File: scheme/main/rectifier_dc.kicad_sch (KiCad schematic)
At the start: 11 parts, among them K1 G2RL-1-E, Q2 BC847

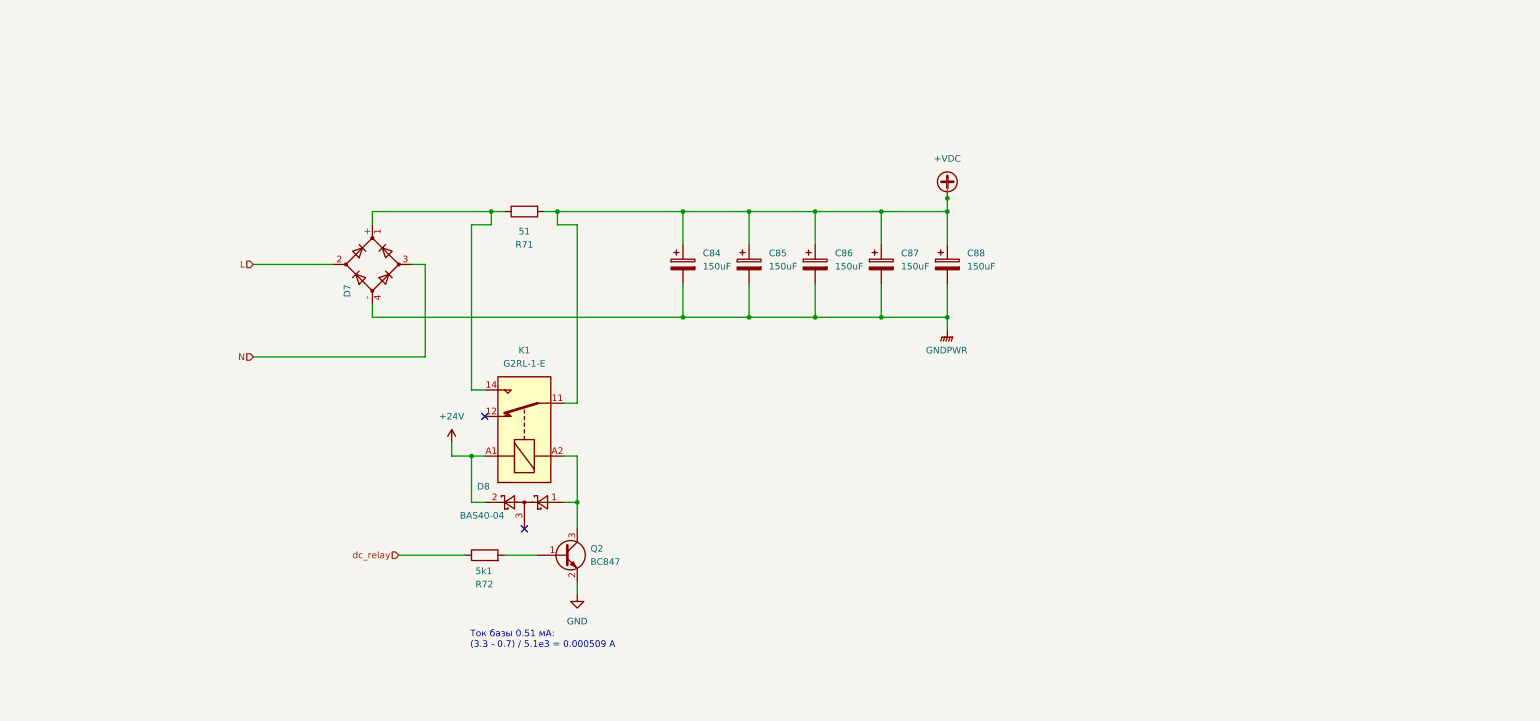
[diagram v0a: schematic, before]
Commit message: drossel in dc+ rail scheme
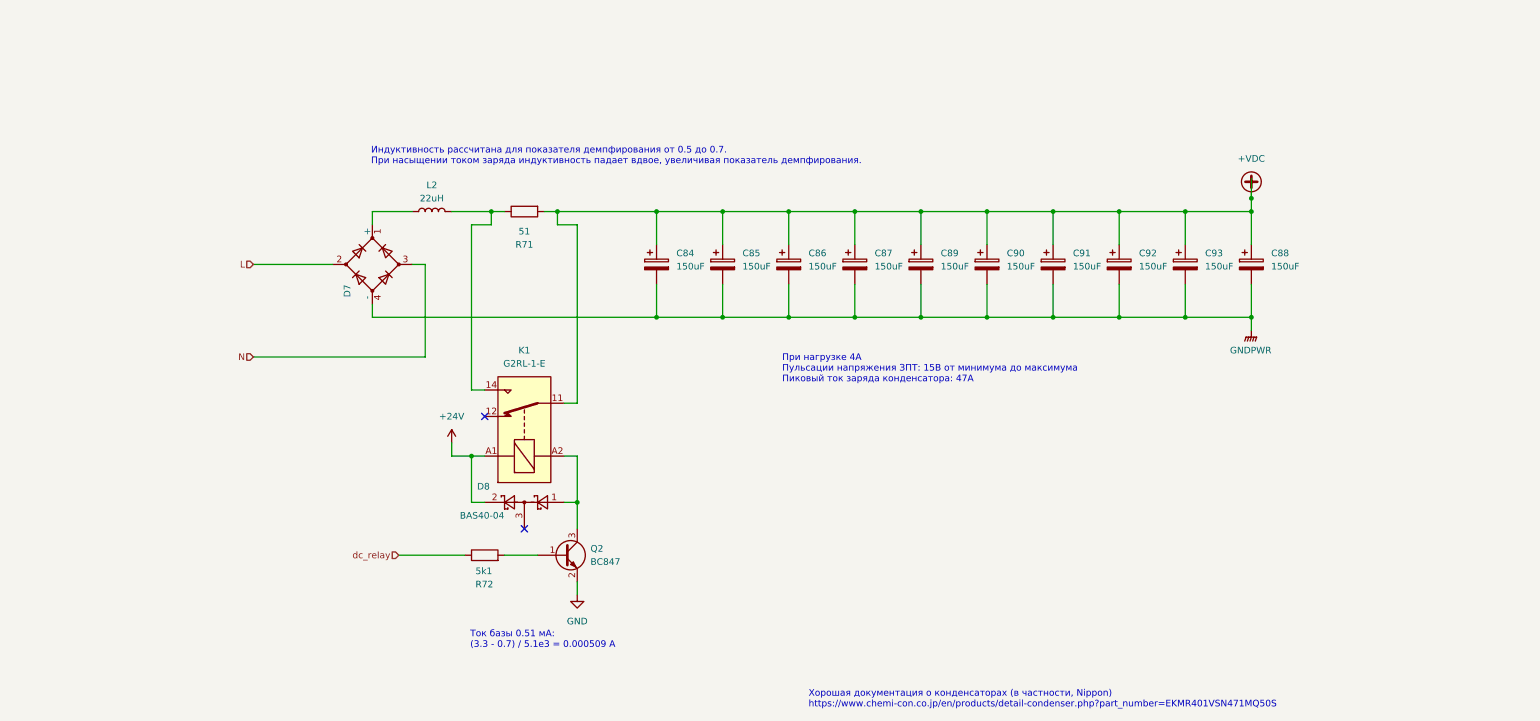
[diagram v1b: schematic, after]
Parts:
- added C89, C90, C91, C92, C93: 150uF, Capacitor_THT:CP_Radial_D30.0mm_P10.00mm_SnapIn, symbol Device:C_Polarized
- added L2: 22uH, Inductor_SMD:L_Vishay_IHLP-6767, symbol Device:L
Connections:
- net +VDC: now also C89.1, C90.1, C91.1, C92.1, C93.1
- net GNDPWR: now also C89.2, C90.2, C91.2, C92.2, C93.2
- net at K1.14, R71.1: now also L2.2; no longer D7.1 (+)
- new net: D7.1 (+), L2.1
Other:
- note added: "Индуктивность рассчитана для показателя демпфирования от 0.5 до 0.7. При насыщении током заряда индуктивность падает вдвое, увеличивая показатель демпфирования."
- note added: "При нагрузке 4А Пульсации напряжения ЗПТ: 15В от минимума до максимума Пиковый ток заряда конденсатора: 47А"
- note added: "Хорошая документация о конденсаторах (в частности, Nippon) https://www.chemi-con.co.jp/en/products/detail-condenser.php?part_number=EKMR401VSN471MQ50S"
- moved on the sheet: C84, C85, C86, C87, C88

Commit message: digital in & out schematic
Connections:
- net +24V: now also D8.3
- no-connect marks 2 -> 1
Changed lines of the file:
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@@
+	)
+	(junction
+		(at 116.84 121.92)
+		(diameter 0)
+		(color 0 0 0 0)
 	)
 	(junction
@@
 		(diameter 0)
 		(color 0 0 0 0)
-	)
-	(no_connect
-		(at 124.46 127)
 	)
 	(no_connect
@@
 	(wire
 		(pts
+			(xy 124.46 127) (xy 116.84 127)
+		)
+		(stroke
+			(width 0)
+			(type default)
+		)
+	)
+	(wire
+		(pts
 			(xy 149.86 86.36) (xy 149.86 80.01)
 		)
@@
 		)
 		(stroke
+			(width 0)
+			(type default)
+		)
+	)
+	(wire
+		(pts
+			(xy 116.84 127) (xy 116.84 121.92)
+		)
+		(stroke

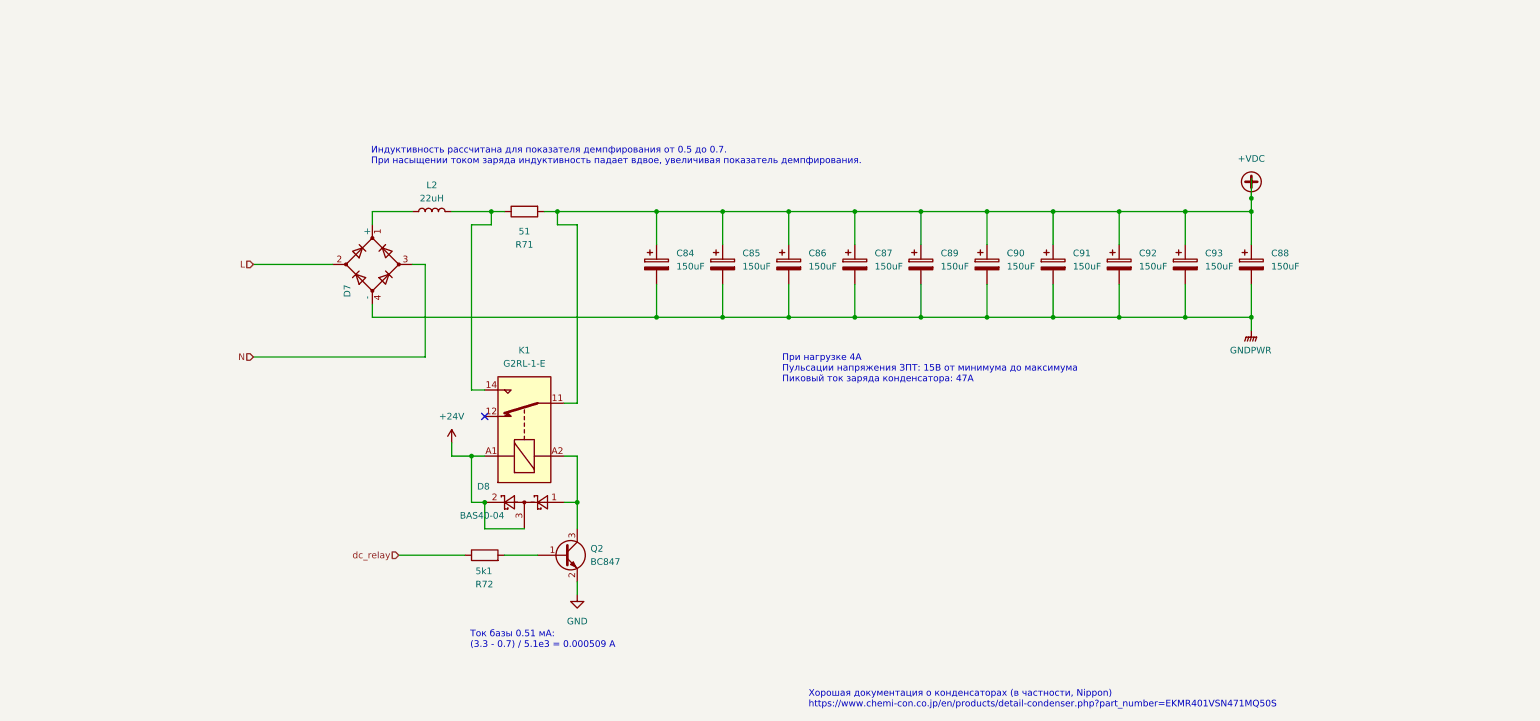
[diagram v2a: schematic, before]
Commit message: dc passive discharge schematic
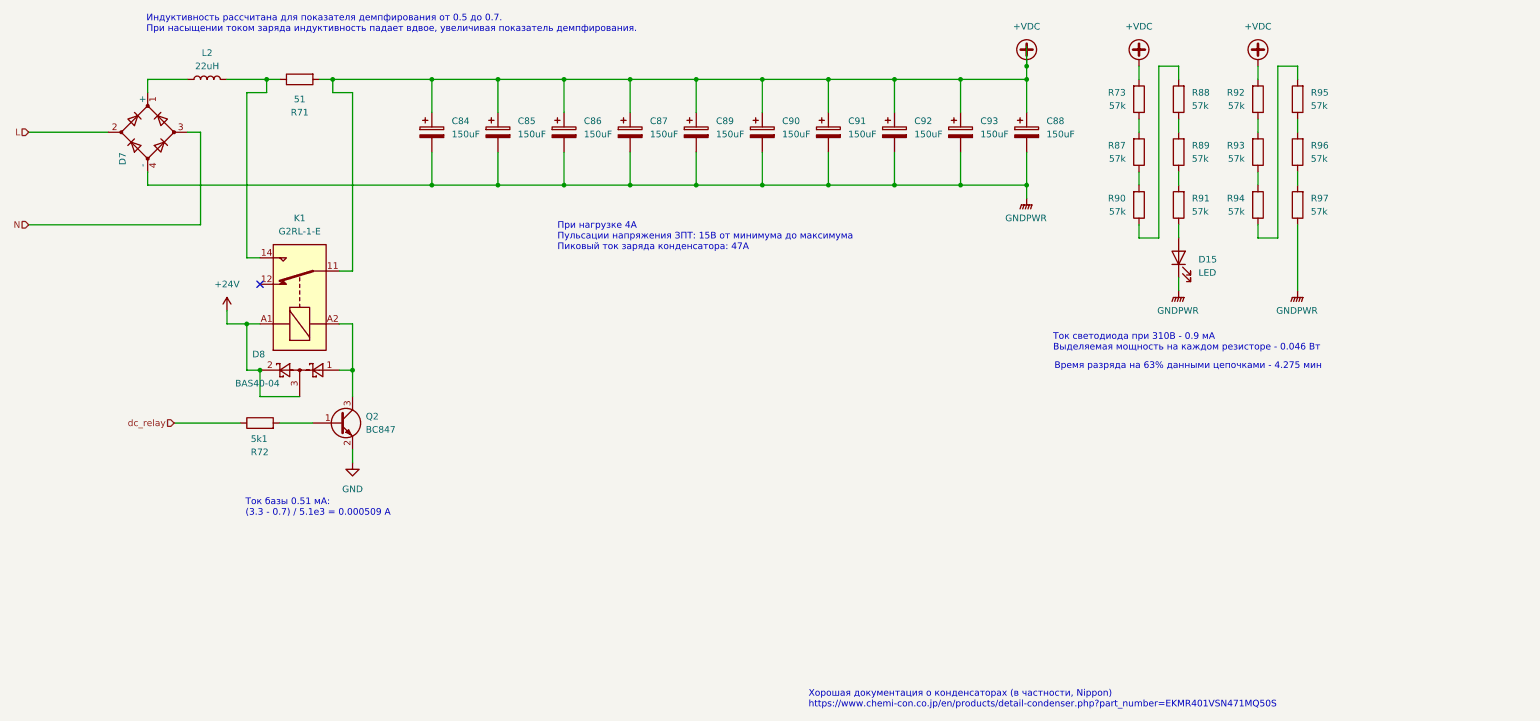
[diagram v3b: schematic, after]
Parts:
- added D15: LED, symbol Device:LED
- added R73, R87, R88, R89, R90, R91, R92, R93, R94, R95, R96, R97: 57k, Resistor_SMD:R_1206_3216Metric, symbol Device:R
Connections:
- net +VDC: now also R73.2, R92.2
- net GNDPWR: now also D15.1 (K), R97.1
- new net: R88.2, R90.1
- new net: R87.1, R90.2
- new net: R89.1, R91.2
- new net: R88.1, R89.2
- new net: R96.1, R97.2
- new net: R92.1, R93.2
- new net: D15.2 (A), R91.1
- new net: R95.1, R96.2
- new net: R94.1, R95.2
- new net: R93.1, R94.2
- new net: R73.1, R87.2
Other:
- note added: "Время разряда на 63% данными цепочками - 4.275 мин"
- note added: "Ток светодиода при 310В - 0.9 мА Выделяемая мощность на каждом резисторе - 0.046 Вт"
- moved on the sheet: C84, C85, C86, C87, C88, C89, C90, C91, C92, C93, D7, D8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
